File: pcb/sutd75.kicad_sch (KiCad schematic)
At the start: 43 parts, among them J1 SWD Header, J2 UART header, J3 USB_C_Receptacle_USB2.0, J4 I2C header, SW1 BOOT0, SW2 BOOT1, SW3 RESET, U1 XC6206PxxxMR, U2 STM32F103RBTx, U3 USBLC6-2SC6

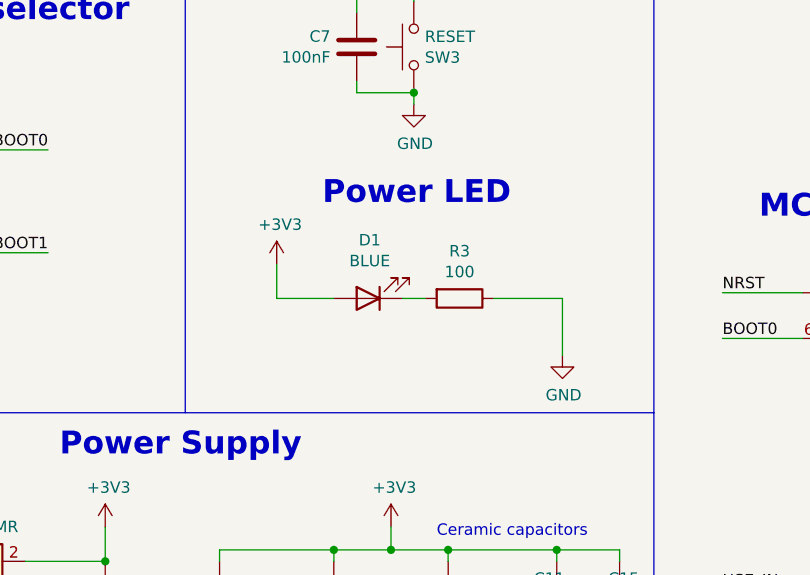
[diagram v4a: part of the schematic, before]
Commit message: Add solder bridge for power led, add silkscreen for pin headers
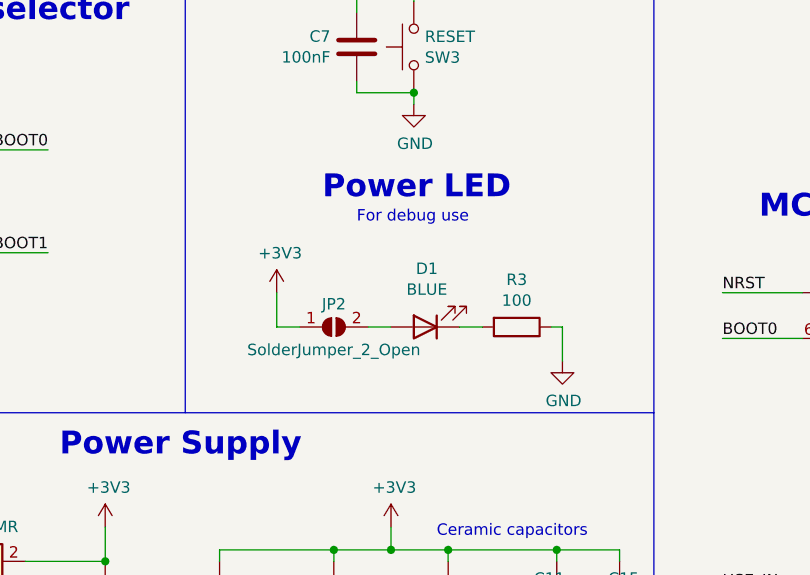
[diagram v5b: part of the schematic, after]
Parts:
- added JP2: SolderJumper_2_Open, Jumper:SolderJumper-2_P1.3mm_Open_RoundedPad1.0x1.5mm, symbol Jumper:SolderJumper_2_Open
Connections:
- net +3V3: now also JP2.1 (A); no longer D1.2 (A)
- new net: D1.2 (A), JP2.2 (B)
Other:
- note added: "For debug use"
- moved on the sheet: D1, R3
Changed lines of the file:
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@@
     (stroke (width 0) (type default) (color 0 0 0 0))
   )
-  (wire (pts (xy 73.66 55.245) (xy 73.66 59.055))
-    (stroke (width 0) (type default) (color 0 0 0 0))
-  )
-  (wire (pts (xy 105.41 59.055) (xy 105.41 65.405))
+  (wire (pts (xy 73.66 58.42) (xy 73.66 62.23))
+    (stroke (width 0) (type default) (color 0 0 0 0))
+  )
+  (wire (pts (xy 105.41 62.23) (xy 105.41 66.04))
     (stroke (width 0) (type default) (color 0 0 0 0))
   )
@@
     (stroke (width 0) (type default) (color 0 0 0 0))
   )
+  (wire (pts (xy 83.82 62.23) (xy 86.36 62.23))
+    (stroke (width 0) (type default) (color 0 0 0 0))
+  )
   (wire (pts (xy 157.48 44.45) (xy 157.48 45.72))
     (stroke (width 0) (type default) (color 0 0 0 0))
@@
     (stroke (width 0) (type default) (color 0 0 0 0))
   )
-  (wire (pts (xy 97.79 59.055) (xy 105.41 59.055))
+  (wire (pts (xy 104.14 62.23) (xy 105.41 62.23))
     (stroke (width 0) (type default) (color 0 0 0 0))
   )
@@
     (stroke (width 0) (type default) (color 0 0 0 0))
   )
+  (wire (pts (xy 73.66 62.23) (xy 76.2 62.23))
+    (stroke (width 0) (type default) (color 0 0 0 0))
+  )
   (wire (pts (xy 53.34 144.78) (xy 53.34 143.51))
     (stroke (width 0) (type default) (color 0 0 0 0))
@@
     (stroke (width 0) (type default) (color 0 0 0 0))
   )
-  (wire (pts (xy 87.63 59.055) (xy 90.17 59.055))
+  (wire (pts (xy 93.98 62.23) (xy 96.52 62.23))
     (stroke (width 0) (type default) (color 0 0 0 0))
   )
@@
   )
   (wire (pts (xy 232.41 129.54) (xy 224.79 129.54))
-    (stroke (width 0) (type default) (color 0 0 0 0))
-  )
-  (wire (pts (xy 73.66 59.055) (xy 80.01 59.055))
     (stroke (width 0) (type default) (color 0 0 0 0))
   )
@@
     (effects (font (size 1.27 1.27)) (justify left bottom))
   )
+  (text "For debug use" (at 82.55 50.8 0)
+    (effects (font (size 1.27 1.27)) (justify left bottom))
+  )
   (text "C_load = 20pF\nR_s = 80Ω" (at 50.8 129.54 0)
     (effects (font (size 1.27 1.27)) (justify left bottom))
@@
     (effects (font (size 2.54 2.54) (thickness 0.508) bold) (justify left bottom))
   )
-  (text "Power LED" (at 78.74 48.895 0)
+  (text "Power LED" (at 78.74 48.26 0)
     (effects (font (size 2.54 2.54) (thickness 0.508) bold) (justify left bottom))
   )
@@
     )
     (pin "1")
+  )
+  (symbol (lib_id "Jumper:SolderJumper_2_Open") (at 80.01 62.23 0) (mirror x) (unit 1)
+    (in_bom yes) (on_board yes)
+    (property "Reference" "JP2" (id 0) (at 80.01 59.69 0))
+    (property "Value" "SolderJumper_2_Open" (id 1) (at 80.01 64.77 0))
+    (property "Footprint" "Jumper:SolderJumper-2_P1.3mm_Open_RoundedPad1.0x1.5mm" (id 2) (at 80.01 62.23 0)
+      (effects (font (size 1.27 1.27)) hide)
+    )
+    (property "Datasheet" "~" (id 3) (at 80.01 62.23 0)
+      (effects (font (size 1.27 1.27)) hide)
+    )
+    (pin "1")
+    (pin "2")
   )
   (symbol (lib_id "Device:R") (at 45.72 139.7 0) (unit 1)
@@
     (pin "6")
   )
-  (symbol (lib_id "power:GND") (at 105.41 65.405 0) (unit 1)
-    (in_bom yes) (on_board yes)
-    (property "Reference" "#PWR0106" (id 0) (at 105.41 71.755 0)
-      (effects (font (size 1.27 1.27)) hide)
-    )
-    (property "Value" "GND" (id 1) (at 105.537 69.7992 0))
-    (property "Footprint" "" (id 2) (at 105.41 65.405 0)
-      (effects (font (size 1.27 1.27)) hide)
-    )
-    (property "Datasheet" "" (id 3) (at 105.41 65.405 0)
+  (symbol (lib_id "power:GND") (at 105.41 66.04 0) (unit 1)
+    (in_bom yes) (on_board yes)
+    (property "Reference" "#PWR0106" (id 0) (at 105.41 72.39 0)
+      (effects (font (size 1.27 1.27)) hide)
+    )
+    (property "Value" "GND" (id 1) (at 105.537 70.4342 0))
+    (property "Footprint" "" (id 2) (at 105.41 66.04 0)
+      (effects (font (size 1.27 1.27)) hide)
+    )
+    (property "Datasheet" "" (id 3) (at 105.41 66.04 0)
       (effects (font (size 1.27 1.27)) hide)
     )
@@
     (pin "3")
   )
-  (symbol (lib_id "Device:LED") (at 83.82 59.055 180) (unit 1)
-    (in_bom yes) (on_board yes)
-    (property "Reference" "D1" (id 0) (at 83.9978 52.578 0))
-    (property "Value" "BLUE" (id 1) (at 83.9978 54.8894 0))
-    (property "Footprint" "LED_SMD:LED_0603_1608Metric" (id 2) (at 83.82 59.055 0)
-      (effects (font (size 1.27 1.27)) hide)
-    )
-    (property "Datasheet" "~" (id 3) (at 83.82 59.055 0)
-      (effects (font (size 1.27 1.27)) hide)
-    )
-    (property "LSCS" "C72041" (id 4) (at 83.82 59.055 0)
+  (symbol (lib_id "Device:LED") (at 90.17 62.23 180) (unit 1)
+    (in_bom yes) (on_board yes)
+    (property "Reference" "D1" (id 0) (at 90.3478 55.753 0))
+    (property "Value" "BLUE" (id 1) (at 90.3478 58.0644 0))
+    (property "Footprint" "LED_SMD:LED_0603_1608Metric" (id 2) (at 90.17 62.23 0)
+      (effects (font (size 1.27 1.27)) hide)
+    )
+    (property "Datasheet" "~" (id 3) (at 90.17 62.23 0)
+      (effects (font (size 1.27 1.27)) hide)
+    )
+    (property "LSCS" "C72041" (id 4) (at 90.17 62.23 0)
       (effects (font (size 1.27 1.27)) hide)
     )
@@
     (pin "1")
   )
-  (symbol (lib_id "Device:R") (at 93.98 59.055 270) (unit 1)
-    (in_bom yes) (on_board yes)
-    (property "Reference" "R3" (id 0) (at 93.98 53.7972 90))
-    (property "Value" "100" (id 1) (at 93.98 56.1086 90))
-    (property "Footprint" "Resistor_SMD:R_0603_1608Metric" (id 2) (at 93.98 57.277 90)
-      (effects (font (size 1.27 1.27)) hide)
-    )
-    (property "Datasheet" "~" (id 3) (at 93.98 59.055 0)
-      (effects (font (size 1.27 1.27)) hide)
-    )
-    (property "LSCS" "C22775" (id 4) (at 93.98 59.055 0)
+  (symbol (lib_id "Device:R") (at 100.33 62.23 270) (unit 1)
+    (in_bom yes) (on_board yes)
+    (property "Reference" "R3" (id 0) (at 100.33 56.9722 90))
+    (property "Value" "100" (id 1) (at 100.33 59.2836 90))
+    (property "Footprint" "Resistor_SMD:R_0603_1608Metric" (id 2) (at 100.33 60.452 90)
+      (effects (font (size 1.27 1.27)) hide)
+    )
+    (property "Datasheet" "~" (id 3) (at 100.33 62.23 0)
+      (effects (font (size 1.27 1.27)) hide)
+    )
+    (property "LSCS" "C22775" (id 4) (at 100.33 62.23 0)
       (effects (font (size 1.27 1.27)) hide)
     )
@@
     (pin "1")
   )
-  (symbol (lib_id "power:+3V3") (at 73.66 55.245 0) (unit 1)
-    (in_bom yes) (on_board yes)
-    (property "Reference" "#PWR0101" (id 0) (at 73.66 59.055 0)
-      (effects (font (size 1.27 1.27)) hide)
-    )
-    (property "Value" "+3V3" (id 1) (at 74.041 50.8508 0))
-    (property "Footprint" "" (id 2) (at 73.66 55.245 0)
-      (effects (font (size 1.27 1.27)) hide)
-    )
-    (property "Datasheet" "" (id 3) (at 73.66 55.245 0)
+  (symbol (lib_id "power:+3V3") (at 73.66 58.42 0) (unit 1)
+    (in_bom yes) (on_board yes)
+    (property "Reference" "#PWR0101" (id 0) (at 73.66 62.23 0)
+      (effects (font (size 1.27 1.27)) hide)
+    )
+    (property "Value" "+3V3" (id 1) (at 74.041 54.0258 0))
+    (property "Footprint" "" (id 2) (at 73.66 58.42 0)
+      (effects (font (size 1.27 1.27)) hide)
+    )
+    (property "Datasheet" "" (id 3) (at 73.66 58.42 0)
       (effects (font (size 1.27 1.27)) hide)
     )
@@
     )
     (path "/013f24c9-7bb6-42ab-9020-39cd15d27f83/4ca2ff3c-2786-4b1e-a9d5-675bd4c3958c"
-      (reference "H1") (unit 1) (value "LShift") (footprint "Mounting_Keyboard_Stabilizer:Stabilizer_Cherry_MX_2u")
+      (reference "H1") (unit 1) (value "LShift") (footprint "Mounting_Keyboard_Stabilizer:Stabilizer_Cherry_MX_2.00u")
     )
     (path "/013f24c9-7bb6-42ab-9020-39cd15d27f83/9ad81d7d-e387-445d-9f51-21b23583c662"
@@
     )
     (path "/013f24c9-7bb6-42ab-9020-39cd15d27f83/80a5ce93-6b27-4c98-9b42-317a65befd8f"
-      (reference "H3") (unit 1) (value "Enter") (footprint "Mounting_Keyboard_Stabilizer:Stabilizer_Cherry_MX_2u")
+      (reference "H3") (unit 1) (value "Enter") (footprint "Mounting_Keyboard_Stabilizer:Stabilizer_Cherry_MX_2.00u")
     )
     (path "/013f24c9-7bb6-42ab-9020-39cd15d27f83/aff22344-93dd-4b7c-85f4-79a3ff513fba"
-      (reference "H4") (unit 1) (value "Backspace") (footprint "Mounting_Keyboard_Stabilizer:Stabilizer_Cherry_MX_2u")
+      (reference "H4") (unit 1) (value "Backspace") (footprint "Mounting_Keyboard_Stabilizer:Stabilizer_Cherry_MX_2.00u")
     )
     (path "/664824cf-504f-4214-b773-897636e5ed26"
@@
       (reference "JP1") (unit 1) (value "SolderJumper_2_Open") (footprint "Jumper:SolderJumper-2_P1.3mm_Open_RoundedPad1.0x1.5mm")
     )
+    (path "/11176cf7-8219-4eb6-8cff-2d29f76f4948"
+      (reference "JP2") (unit 1) (value "SolderJumper_2_Open") (footprint "Jumper:SolderJumper-2_P1.3mm_Open_RoundedPad1.0x1.5mm")
+    )
     (path "/135d4eac-1100-497c-a29d-1756be180bb9"
